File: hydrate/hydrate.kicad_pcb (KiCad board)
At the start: 2 copper layers, 1 part, among them U1 K32L2Bx1VFM0A

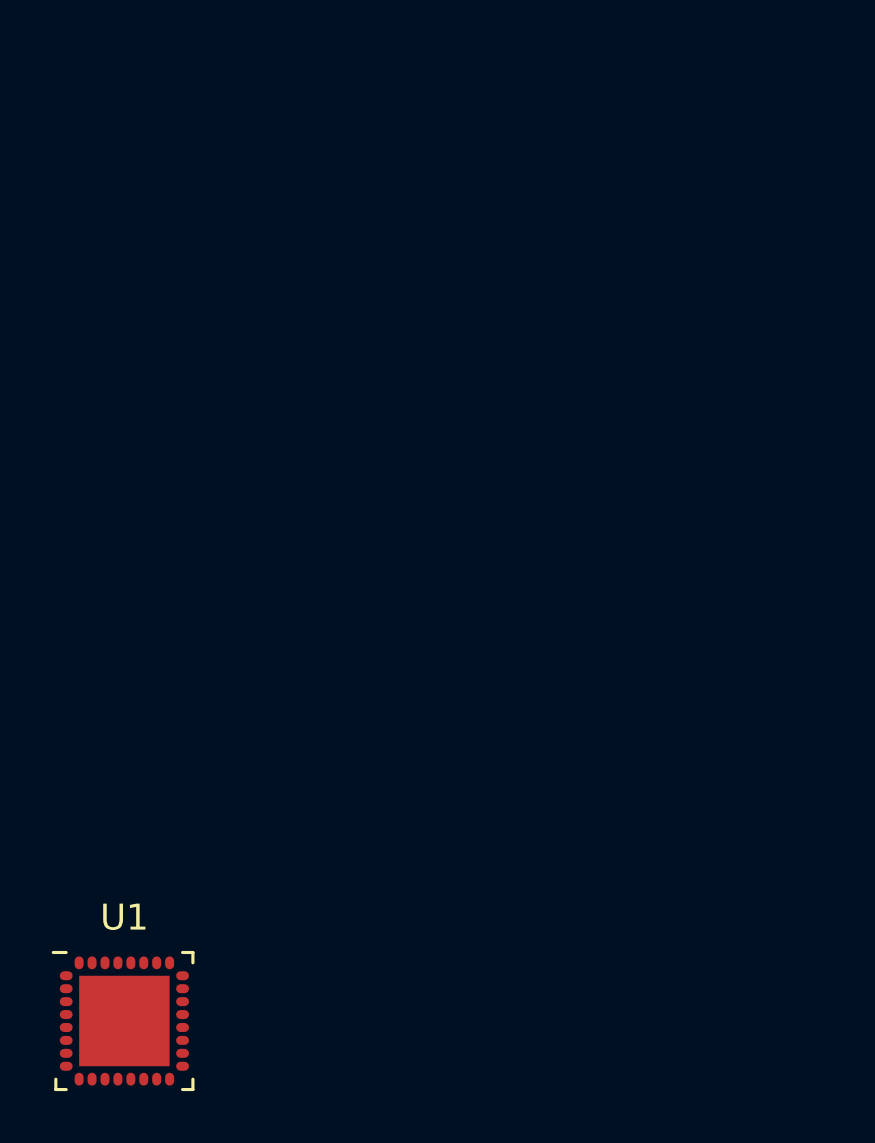
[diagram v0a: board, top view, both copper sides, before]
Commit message: Saving place. MCU and power management ICs added
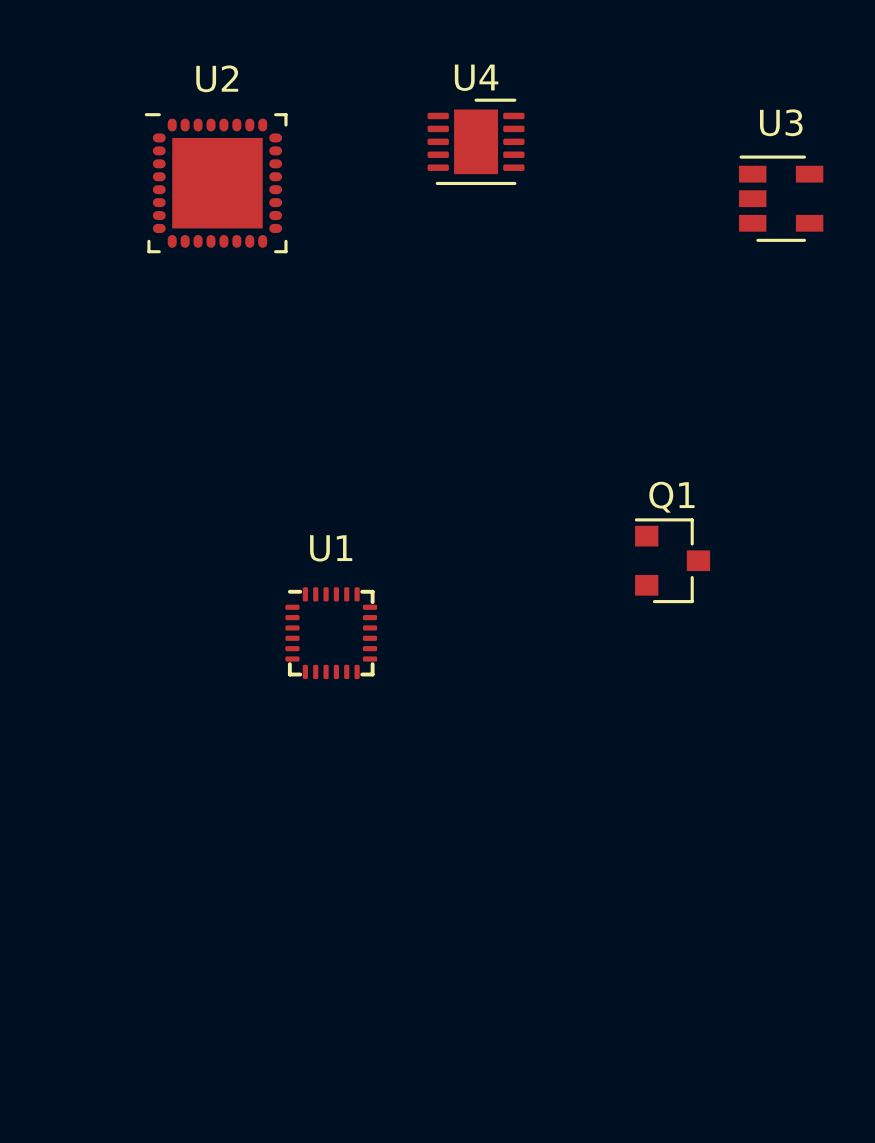
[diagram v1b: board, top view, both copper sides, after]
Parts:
- added Q1: DMP3099L-7, Package_TO_SOT_SMD:SOT-23, F.Cu at (143.4, 76.0)
- added U2: K32L2Bx1VFM0A, hydrate:QFN-32_EP_5x5_Pitch0.5mm, F.Cu at (125.8, 61.4)
- added U3: MCP73832-2-OT, Package_TO_SOT_SMD:SOT-23-5, F.Cu at (147.6, 62.0)
- added U4: LTC3536IDD, hydrate:DFN-10-1EP_3x3mm_P0.5mm_EP0.25x0.70mm, F.Cu at (135.8, 59.8)
- U1: value K32L2Bx1VFM0A -> ICM-20948; footprint hydrate:QFN-32_EP_5x5_Pitch0.5mm -> Sensor_Motion:InvenSense_QFN-24_3x3mm_P0.4mm
- moved U1 17.0 mm to (130.2, 78.8)
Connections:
- U1 pad 20: Net-(U1-Pad20) -> Net-(U1-Pad18)

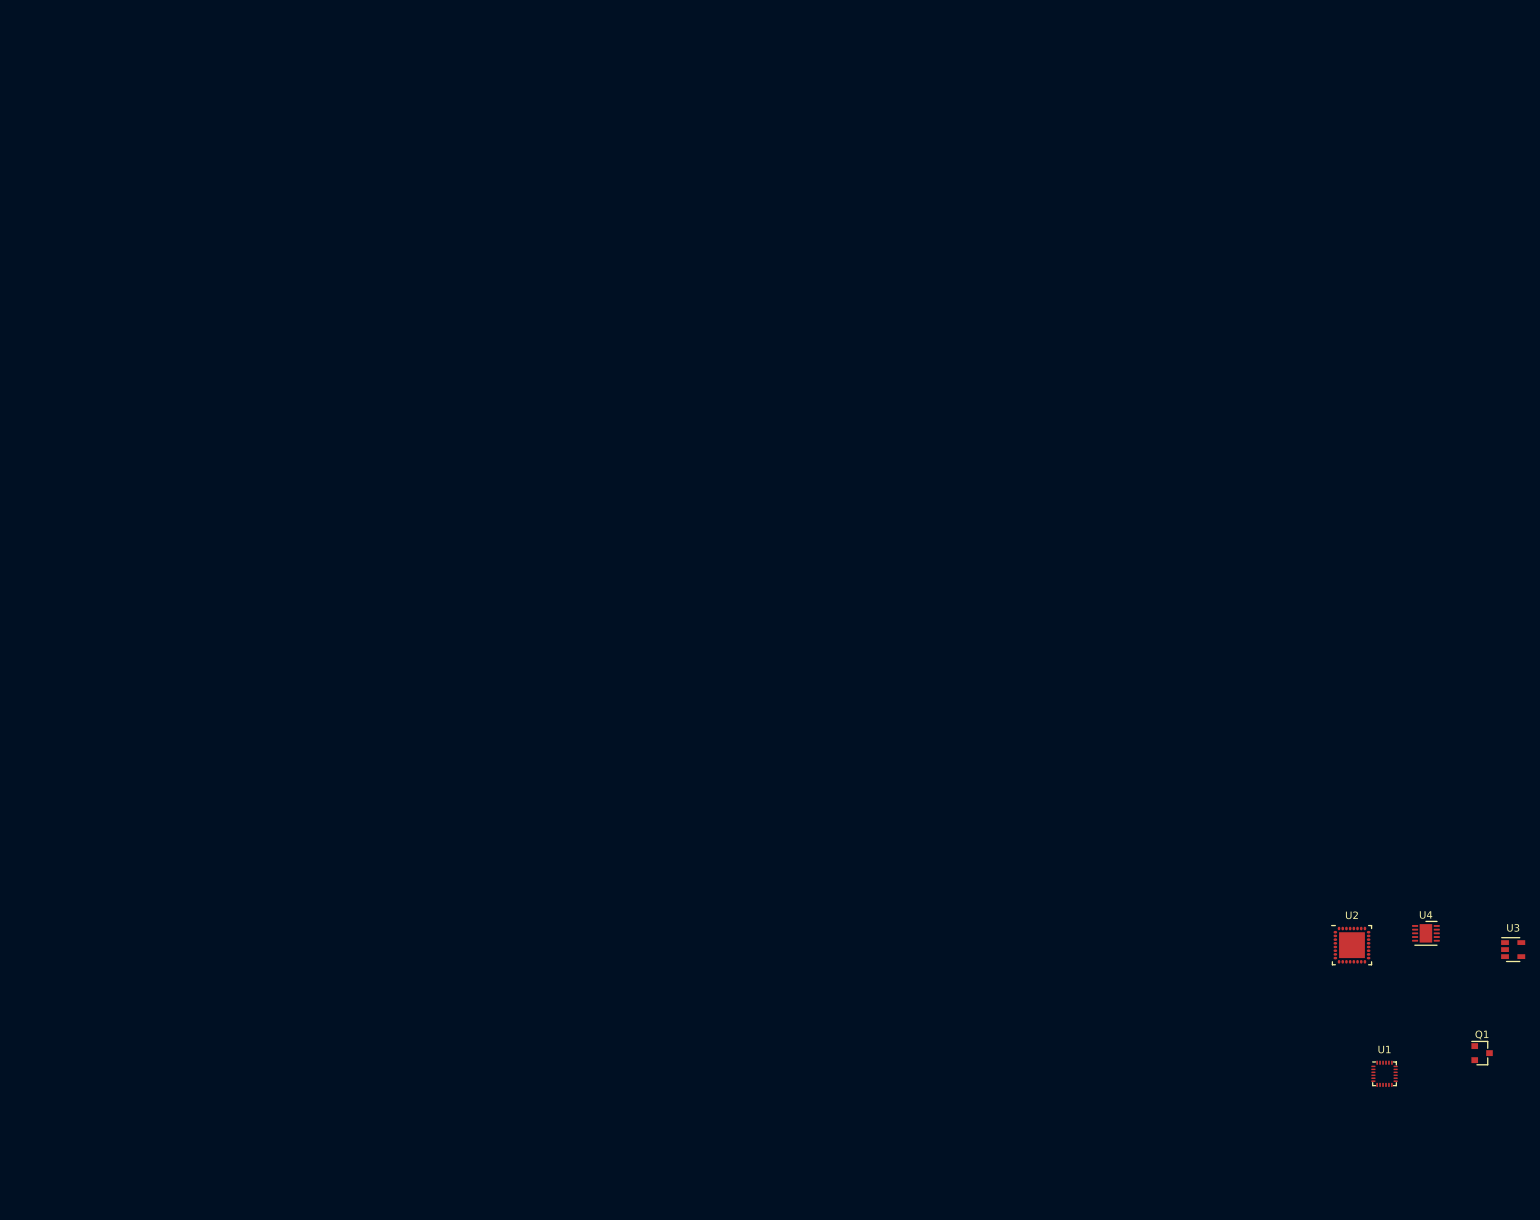
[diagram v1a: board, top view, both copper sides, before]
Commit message: Began layout of Switcher and Battery charger on backside of board
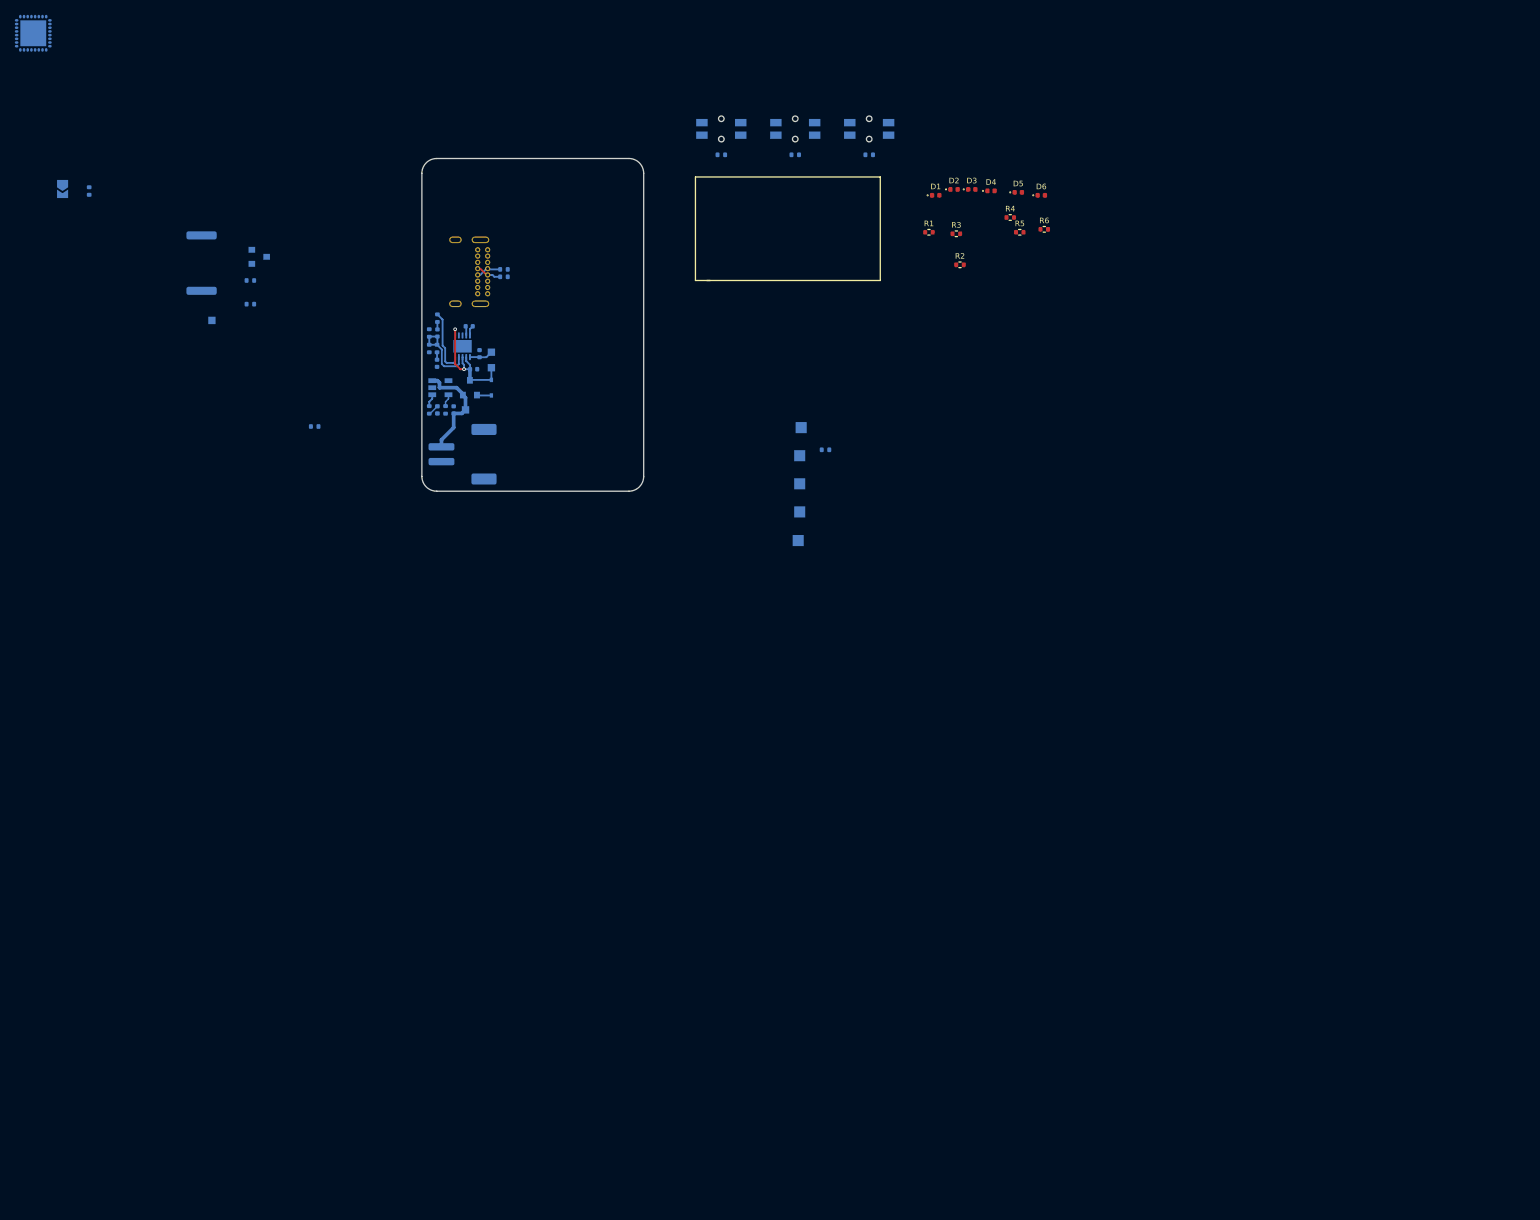
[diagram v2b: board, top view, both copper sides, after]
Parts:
- added C1: 4.7u, Capacitor_SMD:C_0402_1005Metric, B.Cu at (4.30, -11.0)
- added C2: 22u, Capacitor_SMD:C_0402_1005Metric, B.Cu at (7.80, -18.6)
- added C3: 10u, Capacitor_SMD:C_0402_1005Metric, B.Cu at (7.00, -16.5)
- added C4: 220p, Capacitor_SMD:C_0402_1005Metric, B.Cu at (2.10, -21.4)
- added C5: 47p, Capacitor_SMD:C_0402_1005Metric, B.Cu at (2.05, -17.3)
- added D1: B, LED_SMD:LED_0402_1005Metric, F.Cu at (69.5, -40.0)
- added D2: B, LED_SMD:LED_0402_1005Metric, F.Cu at (72.0, -40.8)
- added D3: B, LED_SMD:LED_0402_1005Metric, F.Cu at (74.4, -40.8)
- added D4: B, LED_SMD:LED_0402_1005Metric, F.Cu at (77.0, -40.6)
- added D5: B, LED_SMD:LED_0402_1005Metric, F.Cu at (80.7, -40.4)
- added D6: B, LED_SMD:LED_0402_1005Metric, F.Cu at (83.8, -40.0)
- added D7: BAT54HT1G, Diode_SMD:D_SOD-323, B.Cu at (9.40, -14.0)
- added D8: B, LED_SMD:LED_0402_1005Metric, B.Cu at (2.10, -11.0)
- added J1: USB_C_Receptacle_USB2.0, Connector_USB:USB_C_Receptacle_GCT_USB4085, B.Cu at (8.90, -26.7)
- added J2: JST_BATT_IN, Connector_JST:JST_PH_S2B-PH-SM4-TB_1x02-1MP_P2.00mm_Horizontal, B.Cu at (5.50, -5.00)
- added JP1: Jumper_NO_Small, Jumper:SolderJumper-2_P1.3mm_Open_TrianglePad1.0x1.5mm, B.Cu at (-48.6, -40.9)
- added L1: 4.7u, Capacitor_SMD:C_0402_1005Metric, B.Cu at (6.40, -22.3)
- added Q2: DMN3042L, Package_TO_SOT_SMD:SOT-23, B.Cu at (-22.0, -31.7)
- added R1: 470R, Resistor_SMD:R_0402_1005Metric, F.Cu at (68.6, -35.0)
- added R10: 22R, Resistor_SMD:R_0402_1005Metric, B.Cu at (11.1, -30.0)
- added R11: 22R, Resistor_SMD:R_0402_1005Metric, B.Cu at (11.1, -29.0)
- added R12: 10k, Resistor_SMD:R_0402_1005Metric, B.Cu at (-14.5, -8.75)
- added R13: 49.9k, Resistor_SMD:R_0402_1005Metric, B.Cu at (2.10, -23.4)
- added R14: 6.49k, Resistor_SMD:R_0402_1005Metric, B.Cu at (2.05, -19.3)
- added R15: 1M, Resistor_SMD:R_0402_1005Metric, B.Cu at (1.00, -19.3)
- added R16: 221k, Resistor_SMD:R_0402_1005Metric, B.Cu at (1.00, -21.4)
- added R17: 2.5k, Resistor_SMD:R_0402_1005Metric, B.Cu at (3.20, -11.0)
- added R18: 10k, Resistor_SMD:R_0402_1005Metric, B.Cu at (-45.0, -40.6)
- added R19: 10k, Resistor_SMD:R_0402_1005Metric, B.Cu at (-23.2, -25.3)
- added R2: 470R, Resistor_SMD:R_0402_1005Metric, F.Cu at (72.8, -30.6)
- added R20: 10k, Resistor_SMD:R_0402_1005Metric, B.Cu at (54.6, -5.60)
- added R21: 470R, Resistor_SMD:R_0402_1005Metric, B.Cu at (1.00, -11.0)
- added R22: 470R, Resistor_SMD:R_0402_1005Metric, B.Cu at (-23.2, -28.5)
- added R3: 470R, Resistor_SMD:R_0402_1005Metric, F.Cu at (72.3, -34.8)
- added R4: 470R, Resistor_SMD:R_0402_1005Metric, F.Cu at (79.6, -37.0)
- added R5: 470R, Resistor_SMD:R_0402_1005Metric, F.Cu at (80.9, -35.0)
- added R6: 470R, Resistor_SMD:R_0402_1005Metric, F.Cu at (84.2, -35.4)
- added R7: 10k, Resistor_SMD:R_0402_1005Metric, B.Cu at (40.5, -45.5)
- added R8: 10k, Resistor_SMD:R_0402_1005Metric, B.Cu at (50.5, -45.5)
- added R9: 10k, Resistor_SMD:R_0402_1005Metric, B.Cu at (60.5, -45.5)
- added SW1: PB0, Button_Switch_SMD:Panasonic_EVQPUL_EVQPUC, B.Cu at (40.5, -49.0)
- added SW2: PB0, Button_Switch_SMD:Panasonic_EVQPUL_EVQPUC, B.Cu at (50.5, -49.0)
- added SW3: PB0, Button_Switch_SMD:Panasonic_EVQPUL_EVQPUC, B.Cu at (60.5, -49.0)
- added TP1: TestPoint, TestPoint:TestPoint_Pad_1.0x1.0mm, B.Cu at (5.90, -11.0)
- added TP2: TestPoint, TestPoint:TestPoint_Pad_1.0x1.0mm, B.Cu at (9.40, -16.7)
- added TP3: TestPoint, TestPoint:TestPoint_Pad_1.0x1.0mm, B.Cu at (9.40, -18.8)
- added TP4: TestPoint, TestPoint:TestPoint_Pad_1.0x1.0mm, B.Cu at (-28.4, -23.1)
- added TP5: SWD_VCC, TestPoint:TestPoint_Pad_1.5x1.5mm, B.Cu at (50.9, 6.67)
- added TP6: SWD_CLK_TP, TestPoint:TestPoint_Pad_1.5x1.5mm, B.Cu at (51.1, 2.80)
- added TP7: SWD_DIO_TP, TestPoint:TestPoint_Pad_1.5x1.5mm, B.Cu at (51.1, -1.00)
- added TP8: SWD_RESET_TP, TestPoint:TestPoint_Pad_1.5x1.5mm, B.Cu at (51.1, -4.80)
- added TP9: SWD_GND, TestPoint:TestPoint_Pad_1.5x1.5mm, B.Cu at (51.3, -8.60)
- Q1, U2, U3, U4: moved to B.Cu
- U1: value ICM-20948 -> AST0760MCTRQ; footprint Sensor_Motion:InvenSense_QFN-24_3x3mm_P0.4mm -> hydrate:AST0760MCTRQ; moved to B.Cu
- moved U2 216.9 mm to (-52.6, -61.9), turned to 180 degrees
- moved U1 194.0 mm to (-29.8, -30.9)
- moved Q1 163.8 mm to (6.50, -14.0), turned to 90 degrees
- moved U3 163.8 mm to (2.50, -14.0)
- moved U4 152.6 mm to (5.50, -19.6), turned to 270 degrees
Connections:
- net Net-(U2-Pad20) renamed /I2C_SDA
- net Net-(U2-Pad21) renamed /I2C_SCL
- Q1 pad 3: Net-(D7-Pad1) -> Net-(C3-Pad1)
- U2 pad 10: Net-(U2-Pad10) -> /SWD_CLK
- U2 pad 11: Net-(U2-Pad11) -> /BUZZER_PWM
- U2 pad 13: Net-(U2-Pad13) -> /SWD_DIO
- U2 pad 14: Net-(U2-Pad14) -> /BOOTCFG0
- U2 pad 16: Net-(U2-Pad16) -> GND
- U2 pad 19: Net-(U2-Pad19) -> /nRESET
- U2 pad 2: Net-(U2-Pad2) -> GND
- U2 pad 22: Net-(U2-Pad22) -> /LED0
- U2 pad 23: Net-(U2-Pad23) -> /LED1
- U2 pad 24: Net-(U2-Pad24) -> /LED2
- U2 pad 25: Net-(U2-Pad25) -> /LED3
- U2 pad 26: Net-(U2-Pad26) -> /PB0
- U2 pad 27: Net-(U2-Pad27) -> /PB1
- U2 pad 29: Net-(U2-Pad29) -> /LED4
- U2 pad 3: Net-(U2-Pad3) -> /USB_DP
- U2 pad 30: Net-(U2-Pad30) -> /LED5
- U2 pad 31: Net-(U2-Pad31) -> /PB2
- U2 pad 33: Net-(U2-Pad33) -> GND
- U2 pad 4: Net-(U2-Pad4) -> /USB_DM
- U2 pad 6: Net-(U2-Pad6) -> +5V
- U2 pad 8: Net-(U2-Pad8) -> GND
- U3 pad 1: BATT_STAT -> /BATT_STAT
- U4 pad 1: Net-(U4-Pad1) -> Net-(C3-Pad1)
- U4 pad 3: Net-(U4-Pad3) -> GND
- U4 pad 7: Net-(D7-Pad1) -> Net-(C3-Pad1)
- U4 pad 8: Net-(U4-Pad8) -> Net-(C3-Pad1)
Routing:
- net Net-(C3-Pad1): track 0.00 -> 17.6 mm, vias 0 -> 2
- net +BATT: track 0.00 -> 14.7 mm
- net Net-(C4-Pad2): track 0.00 -> 10.7 mm
- net Net-(R13-Pad1): track 0.00 -> 8.90 mm
- net Net-(J1-PadA6): track 0.00 -> 3.50 mm
- net Net-(J1-PadA7): track 0.00 -> 3.43 mm
- net +3V3: track 0.00 -> 3.19 mm
- net +5V: track 0.00 -> 1.97 mm
- net Net-(R17-Pad1): track 0.00 -> 1.71 mm
- net /BATT_STAT: track 0.00 -> 1.71 mm
- net Net-(D8-Pad1): track 0.00 -> 1.51 mm
- net Net-(L1-Pad2): track 0.00 -> 1.39 mm
- net Net-(L1-Pad1): track 0.00 -> 1.27 mm
- net Net-(C4-Pad1): track 0.00 -> 1.01 mm
- net Net-(C5-Pad1): track 0.00 -> 1.01 mm
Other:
- board outline added: 30 x 45 mm
- rule via_min_drill: 0.3 -> 0.25
- rule via_min_size: 0.4 -> 0.3
